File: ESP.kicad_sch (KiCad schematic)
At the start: 39 parts, among them J5 JST-XH, P1 B6B-ZRLFSN, P2 B6B-ZRLFSN, P3 B6B-ZRLFSN, P4 B6B-ZRLFSN, P5 B6B-ZRLFSN, P6 B6B-ZRLFSN, U14 W25Q16JVS, U3 DRV8835DSSR, U4 RP2040, U5 DRV8835DSSR, U6 DRV8835DSSR, Y1 ABM8-272-T3

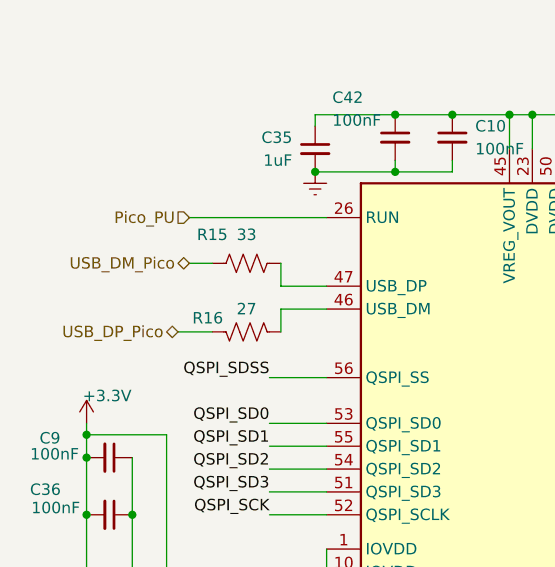
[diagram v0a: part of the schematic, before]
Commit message: Fixing issues
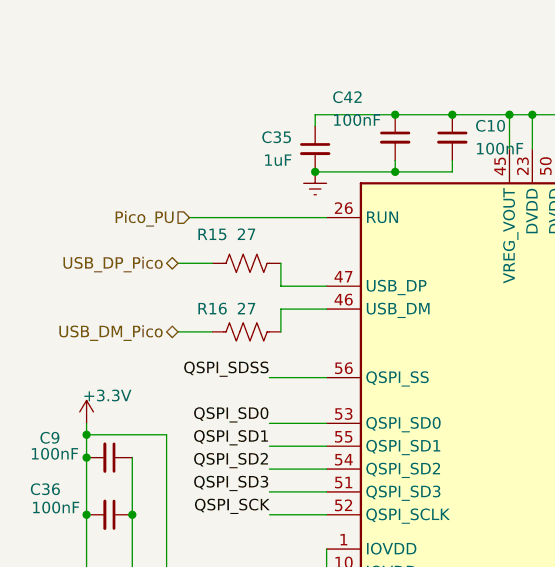
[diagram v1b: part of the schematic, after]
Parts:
- R15: value 33 -> 27
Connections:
- net USB_DM_Pico: now also R16.1; no longer R15.1
- net USB_DP_Pico: now also R15.1; no longer R16.2
- net at U4.46 (USB_DM): now also R16.2; no longer R16.1
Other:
- moved on the sheet: R16
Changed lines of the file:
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@@
 	(wire
 		(pts
-			(xy 30.48 45.72) (xy 33.02 45.72)
+			(xy 29.21 45.72) (xy 33.02 45.72)
 		)
 		(stroke
@@
 	(hierarchical_label "USB_DM_Pico"
 		(shape bidirectional)
-		(at 30.48 45.72 180)
+		(at 29.21 53.34 180)
 		(fields_autoplaced yes)
 		(effects
@@
 	(hierarchical_label "USB_DP_Pico"
 		(shape bidirectional)
-		(at 29.21 53.34 180)
+		(at 29.21 45.72 180)
 		(fields_autoplaced yes)
 		(effects
@@
 	(symbol
 		(lib_id "Device:R_US")
-		(at 36.83 53.34 270)
-		(mirror x)
+		(at 36.83 53.34 90)
 		(unit 1)
 		(exclude_from_sim no)
@@
 		(dnp no)
 		(property "Reference" "R16"
-			(at 32.512 51.816 90)
+			(at 33.02 50.8 90)
 			(effects
 				(font
@@
 		)
 		(property "Footprint" "Resistor_SMD:R_0402_1005Metric"
-			(at 36.576 52.324 90)
+			(at 37.084 52.324 90)
 			(effects
 				(font
@@
 			)
 		)
-		(property "Value" "33"
+		(property "Value" "27"
 			(at 36.83 42.545 90)
 			(effects

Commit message: Rev 2 finished
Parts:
- C10, C14, C33, C36, C37, C38, C39, C40, C42, C7, C8, C9: LCSC Part # C1525 -> C307331
- TP2: footprint (none) -> TestPoint:TestPoint_Pad_D1.5mm
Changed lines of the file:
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@@
 			)
 		)
-		(property "LCSC Part #" "C1525"
+		(property "LCSC Part #" "C307331"
 			(at 21.59 83.82 0)
 			(effects
@@
 			)
 		)
-		(property "Footprint" ""
+		(property "Footprint" "TestPoint:TestPoint_Pad_D1.5mm"
 			(at 105.41 154.94 0)
 			(effects
@@
 			)
 		)
-		(property "LCSC Part #" "C1525"
+		(property "LCSC Part #" "C307331"
 			(at 43.18 158.75 0)
 			(effects
@@
 			)
 		)
-		(property "LCSC Part #" "C1525"
+		(property "LCSC Part #" "C307331"
 			(at 21.59 67.31 0)
 			(effects
@@
 			)
 		)
-		(property "LCSC Part #" "C1525"
+		(property "LCSC Part #" "C307331"
 			(at 21.59 91.44 0)
 			(effects
@@
 			)
 		)
-		(property "LCSC Part #" "C1525"
+		(property "LCSC Part #" "C307331"
 			(at 96.52 29.21 0)
 			(effects
@@
 			)
 		)
-		(property "LCSC Part #" "C1525"
+		(property "LCSC Part #" "C307331"
 			(at 53.34 31.75 0)
 			(effects
@@
 			)
 		)
-		(property "LCSC Part #" "C1525"
+		(property "LCSC Part #" "C307331"
 			(at 59.69 31.75 0)
 			(effects
@@
 			)
 		)
-		(property "LCSC Part #" "C1525"
+		(property "LCSC Part #" "C307331"
 			(at 128.27 67.31 0)
 			(effects
@@
 			)
 		)
-		(property "LCSC Part #" "C1525"
+		(property "LCSC Part #" "C307331"
 			(at 21.59 99.06 0)
 			(effects
@@
 			)
 		)
-		(property "LCSC Part #" "C1525"
+		(property "LCSC Part #" "C307331"
 			(at 21.59 106.68 0)
 			(effects
@@
 			)
 		)
-		(property "LCSC Part #" "C1525"
+		(property "LCSC Part #" "C307331"
 			(at 85.09 24.13 0)
 			(effects
@@
 			)
 		)
-		(property "LCSC Part #" "C1525"
+		(property "LCSC Part #" "C307331"
 			(at 21.59 73.66 0)
 			(effects

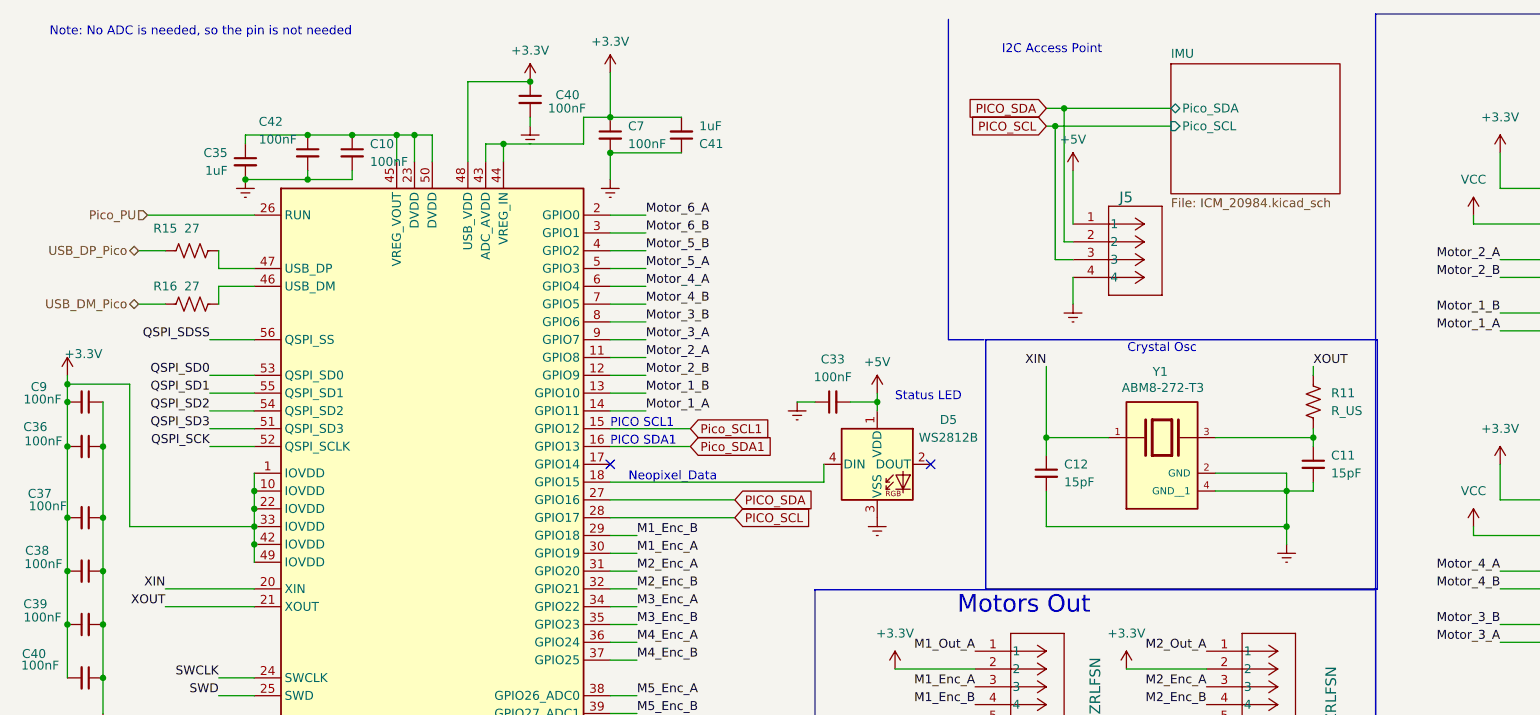
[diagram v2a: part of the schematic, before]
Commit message: Rev 3: fixing I2C and footprints
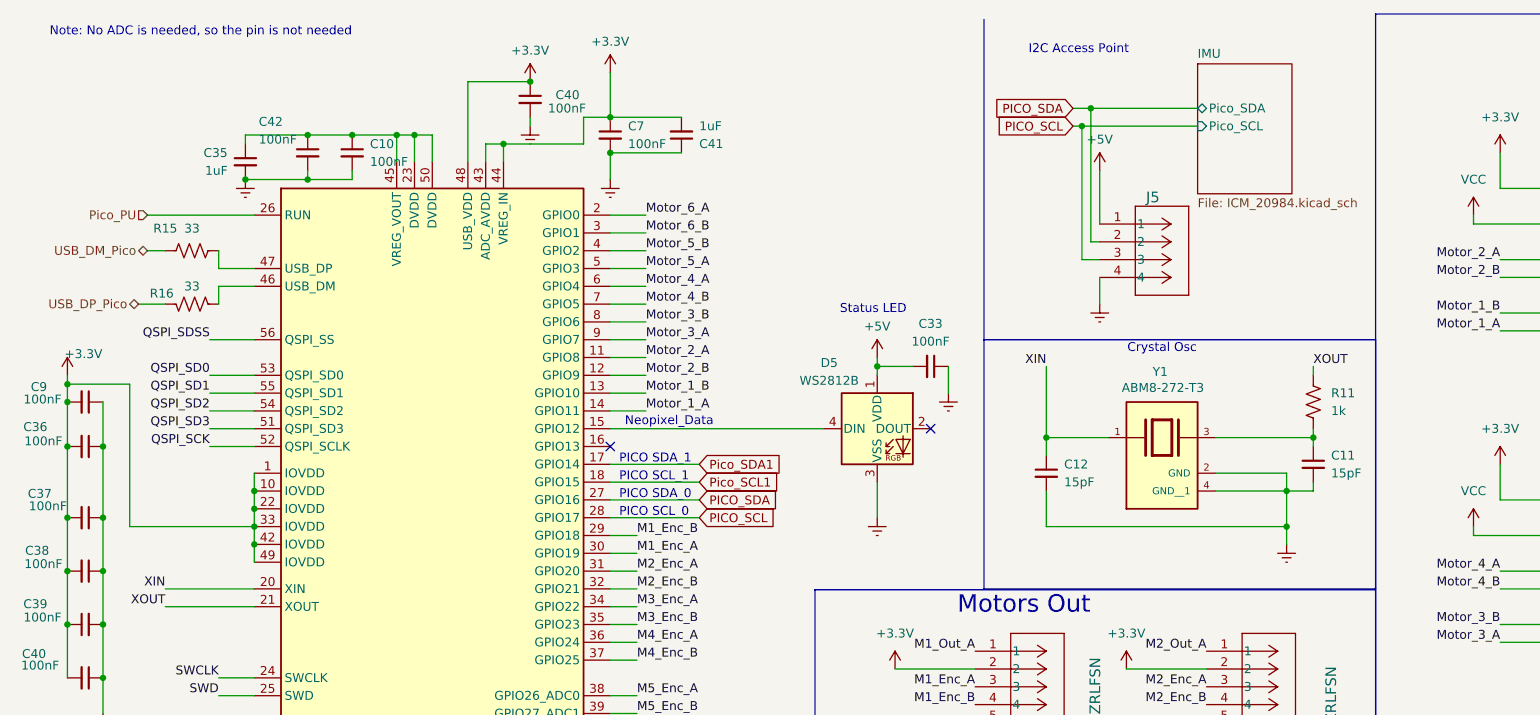
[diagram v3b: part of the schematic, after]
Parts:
- C10, C14, C33, C36, C37, C38, C39, C40, C42, C7, C8, C9: LCSC Part # C307331 -> C1525
- R11: value R_US -> 1k; LCSC Part # (none) -> C11702
- R15, R16: value 27 -> 33
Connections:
- net Pico_SCL1: now also U4.18 (GPIO15); no longer U4.15 (GPIO12)
- net Pico_SDA1: now also U4.17 (GPIO14); no longer U4.16 (GPIO13)
- net USB_DM_Pico: now also R15.1; no longer R16.1
- net USB_DP_Pico: now also R16.2; no longer R15.1
- net at D5.4 (DIN): now also U4.15 (GPIO12); no longer U4.18 (GPIO15)
- net at U4.46 (USB_DM): now also R16.1; no longer R16.2
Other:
- note added: "PICO SCL_0"
- note added: "PICO SCL_1"
- note added: "PICO SDA_0"
- note added: "PICO SDA_1"
- note removed: "PICO SCL1"
- note removed: "PICO SDA1"
- moved on the sheet: C33, D5, J5, R16

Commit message: Cleaning up
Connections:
- net USB_DM_Pico: now also R16.1; no longer R15.1
- net USB_DP_Pico: now also R15.1; no longer R16.2
- net at U4.46 (USB_DM): now also R16.2; no longer R16.1
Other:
- moved on the sheet: R16
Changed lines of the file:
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@@
 	(wire
 		(pts
-			(xy 33.02 53.34) (xy 29.21 53.34)
+			(xy 33.02 53.34) (xy 30.48 53.34)
 		)
 		(stroke
@@
 	(hierarchical_label "USB_DM_Pico"
 		(shape bidirectional)
-		(at 30.48 45.72 180)
+		(at 30.48 53.34 180)
 		(fields_autoplaced yes)
 		(effects
@@
 	(hierarchical_label "USB_DP_Pico"
 		(shape bidirectional)
-		(at 29.21 53.34 180)
+		(at 30.48 45.72 180)
 		(fields_autoplaced yes)
 		(effects
@@
 	(symbol
 		(lib_id "Device:R_US")
-		(at 36.83 53.34 270)
-		(mirror x)
+		(at 36.83 53.34 90)
 		(unit 1)
 		(exclude_from_sim no)
@@
 		(dnp no)
 		(property "Reference" "R16"
-			(at 32.512 51.816 90)
+			(at 31.75 50.8 90)
 			(effects
 				(font
@@
 		)
 		(property "Footprint" "Resistor_SMD:R_0402_1005Metric"
-			(at 36.576 52.324 90)
+			(at 37.084 52.324 90)
 			(effects
 				(font

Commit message: Progress
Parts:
- P1, P2, P3, P4, P5, P6: footprint JST-ZR:CONN_B6B-ZR_JST -> B6B-ZR:CONN_B6B-ZR_JST
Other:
- moved on the sheet: C10, C35, C42

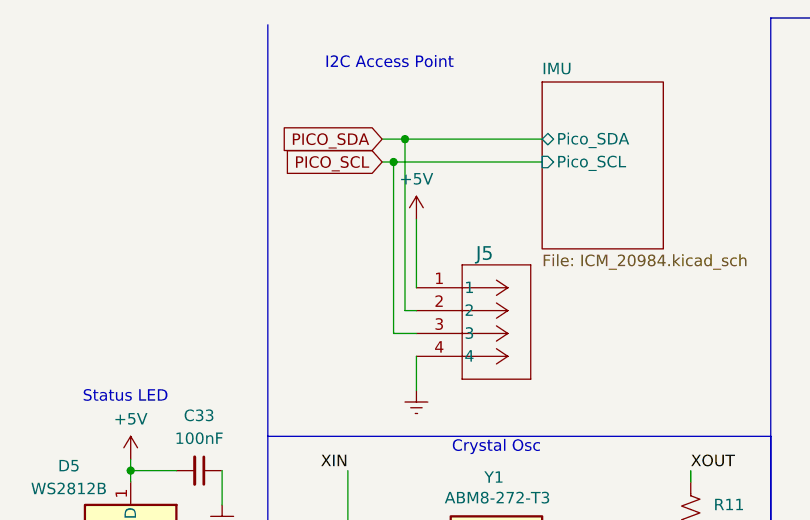
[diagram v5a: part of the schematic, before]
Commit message: Layout for 80x80mm done
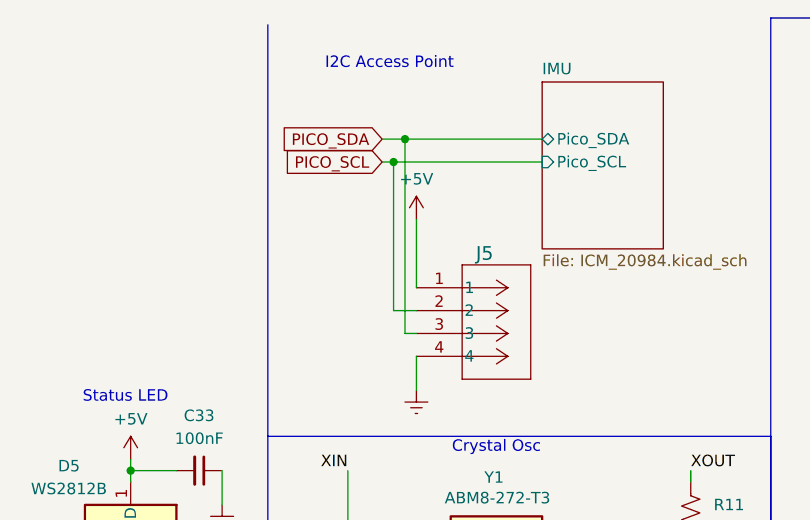
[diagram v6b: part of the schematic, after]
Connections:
- net PICO_SCL: now also J5.2; no longer J5.3
- net PICO_SDA: now also J5.3; no longer J5.2
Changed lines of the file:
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@@
+	(wire
+		(pts
+			(xy 163.83 44.45) (xy 166.37 44.45)
+		)
+		(stroke
+			(width 0)
+			(type default)
+		)
+	)
 	(wire
 		(pts
@@
 	(wire
 		(pts
-			(xy 163.83 27.94) (xy 163.83 46.99)
+			(xy 163.83 27.94) (xy 163.83 44.45)
 		)
 		(stroke
@@
 	(wire
 		(pts
-			(xy 163.83 46.99) (xy 166.37 46.99)
-		)
-		(stroke
-			(width 0)
-			(type default)
-		)
-	)
-	(wire
-		(pts
 			(xy 166.37 34.29) (xy 166.37 41.91)
 		)
@@
 	(wire
 		(pts
-			(xy 165.1 25.4) (xy 165.1 44.45)
+			(xy 165.1 25.4) (xy 165.1 46.99)
 		)
 		(stroke
@@
 	(wire
 		(pts
+			(xy 165.1 46.99) (xy 166.37 46.99)
+		)
+		(stroke
+			(width 0)
+			(type default)
+		)
+	)
+	(wire
+		(pts
 			(xy 19.05 91.44) (xy 19.05 99.06)
 		)
@@
 		)
 		(stroke
-			(width 0)
-			(type default)
-		)
-	)
-	(wire
-		(pts
-			(xy 165.1 44.45) (xy 166.37 44.45)
-		)
-		(stroke

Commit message: Finished new board
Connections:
- net +5V: now also J5.4; no longer J5.1
- net Earth: now also J5.1; no longer J5.4
- net M5_Enc_A: now also U4.39 (GPIO27_ADC1); no longer U4.38 (GPIO26_ADC0)
- net M5_Enc_B: now also U4.38 (GPIO26_ADC0); no longer U4.39 (GPIO27_ADC1)
- net M6_Enc_A: now also U4.41 (GPIO29_ADC3); no longer U4.40 (GPIO28_ADC2)
- net M6_Enc_B: now also U4.40 (GPIO28_ADC2); no longer U4.41 (GPIO29_ADC3)
- net PICO_SCL: now also J5.3; no longer J5.2
- net PICO_SDA: now also J5.2; no longer J5.3
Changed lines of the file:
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@@
 	)
 	(label "M5_Enc_B"
-		(at 100.33 111.76 0)
+		(at 100.33 109.22 0)
 		(fields_autoplaced yes)
 		(effects
@@
 	)
 	(label "M5_Enc_A"
-		(at 100.33 109.22 0)
+		(at 100.33 111.76 0)
 		(fields_autoplaced yes)
 		(effects
@@
 	)
 	(label "M6_Enc_B"
-		(at 100.33 116.84 0)
+		(at 100.33 114.3 0)
 		(fields_autoplaced yes)
 		(effects
@@
 	)
 	(label "M6_Enc_A"
-		(at 100.33 114.3 0)
+		(at 100.33 116.84 0)
 		(fields_autoplaced yes)
 		(effects
@@
 	)
 	(symbol
-		(lib_id "JST-ZH-4Pin:B4B-ZRLFSN")
-		(at 166.37 41.91 0)
-		(unit 1)
-		(exclude_from_sim no)
-		(in_bom yes)
-		(on_board yes)
-		(dnp no)
-		(property "Reference" "J5"
-			(at 172.974 38.1 0)
-			(effects
-				(font
-					(size 1.524 1.524)
-				)
-				(justify left)
-			)
-		)
-		(property "Value" "JST-XH"
-			(at 179.832 46.99 0)
-			(effects
-				(font
-					(size 1.524 1.524)
-				)
-				(justify left)
-				(hide yes)
-			)
-		)
-		(property "Footprint" "Connector_JST:JST_XH_B4B-XH-A_1x04_P2.50mm_Vertical"
-			(at 166.37 41.91 0)
-			(effects
-				(font
-					(size 1.27 1.27)
-					(italic yes)
-				)
-				(hide yes)
-			)
-		)
-		(property "Datasheet" ""
-			(at 166.37 41.91 0)
-			(effects
-				(font
-					(size 1.27 1.27)
-					(italic yes)
-				)
-				(hide yes)
-			)
-		)
-		(property "Description" ""
-			(at 166.37 41.91 0)
-			(effects
-				(font
-					(size 1.27 1.27)
-				)
-				(hide yes)
-			)
-		)
-		(property "JLCPCB Rotation Offset" ""
-			(at 166.37 41.91 0)
-			(effects
-				(font
-					(size 1.27 1.27)
-				)
-				(hide yes)
-			)
-		)
-		(property "LCSC Part # " ""
-			(at 4.191 83.439 0)
-			(effects
-				(font
-					(size 1.27 1.27)
-				)
-				(hide yes)
-			)
-		)
-		(pin "2"
-		)
-		(pin "1"
-		)
-		(pin "3"
-		)
-		(pin "4"
-		)
-		(instances
-			(project "DeltaRhoRobot"
-				(path "/cced1a6d-3dc4-42b2-93bd-998a7b4cf4e8/ff44b13b-7cc8-487d-9bdf-cc68eec5ba2f"
-					(reference "J5")
-					(unit 1)
-				)
-			)
-		)
-	)
-	(symbol
 		(lib_id "power:+3.3V")
 		(at 223.52 76.2 0)
@@
 					(unit 1)
 				)
+			)
+		)
+	)
+	(symbol
+		(lib_id "JST-ZH-4Pin:B4B-ZRLFSN")
+		(at 166.37 49.53 0)
+		(mirror x)
+		(unit 1)
+		(exclude_from_sim no)
+		(in_bom yes)
+		(on_board yes)
+		(dnp no)
+		(property "Reference" "J5"
+			(at 172.974 53.34 0)
+			(effects
+				(font
+					(size 1.524 1.524)
+				)
+				(justify left)
+			)
+		)
+		(property "Value" "JST-XH"
+			(at 179.832 44.45 0)
+			(effects
+				(font
+					(size 1.524 1.524)
+				)
+				(justify left)
+				(hide yes)
+			)
+		)
+		(property "Footprint" "Connector_JST:JST_XH_B4B-XH-A_1x04_P2.50mm_Vertical"
+			(at 166.37 49.53 0)
+			(effects
+				(font
+					(size 1.27 1.27)
+					(italic yes)
+				)
+				(hide yes)
+			)
+		)
+		(property "Datasheet" ""
+			(at 166.37 49.53 0)
+			(effects
+				(font
+					(size 1.27 1.27)
+					(italic yes)
+				)
+				(hide yes)
+			)
+		)
+		(property "Description" ""
+			(at 166.37 49.53 0)
+			(effects
+				(font
+					(size 1.27 1.27)
+				)
+				(hide yes)
+			)
+		)
+		(property "JLCPCB Rotation Offset" ""
+			(at 166.37 49.53 0)
+			(effects
+				(font
+					(size 1.27 1.27)
+				)
+				(hide yes)
+			)
+		)
+		(property "LCSC Part # " ""
+			(at 4.191 8.001 0)
+			(effects
+				(font
+					(size 1.27 1.27)
+				)
+				(hide yes)
+			)
+		)
+		(pin "2"
+		)
+		(pin "1"
+		)
+		(pin "3"
+		)
+		(pin "4"
+		)
+		(instances
+			(project "DeltaRhoRobot"
+				(path "/cced1a6d-3dc4-42b2-93bd-998a7b4cf4e8/ff44b13b-7cc8-487d-9bdf-cc68eec5ba2f"
+					(reference "J5")
+					(unit 1)
+				)

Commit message: Graphics
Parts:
- renumbered C37 to C19, C38 to C20, C42 to C21, C41 to C26, C10 to C27, C7 to C28, C39 to C30, C36 to C32, C14 to C36, C13 to C39, C40 to C42, C35 to C43, C9 to C44, C12 to C45, C33 to C46, C11 to C47, D5 to D4, J5 to J10, P3 to P1, P5 to P3, P6 to P5, P1 to P6, R16 to R13, R15 to R14, R17 to R24, R11 to R25, R18 to R8, U6 to U10, U3 to U11, U4 to U6, U5 to U8, U14 to U9
